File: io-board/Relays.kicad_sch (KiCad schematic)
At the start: 44 parts, among them K1 FRM18A-5 DC12V, K10 FRM18A-5 DC12V, K11 FRM18A-5 DC12V, K2 FRM18A-5 DC12V, K3 FRM18A-5 DC12V, K4 FRM18A-5 DC12V, K5 FRM18A-5 DC12V, K6 FRM18A-5 DC12V, K7 FRM18A-5 DC12V, K8 FRM18A-5 DC12V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

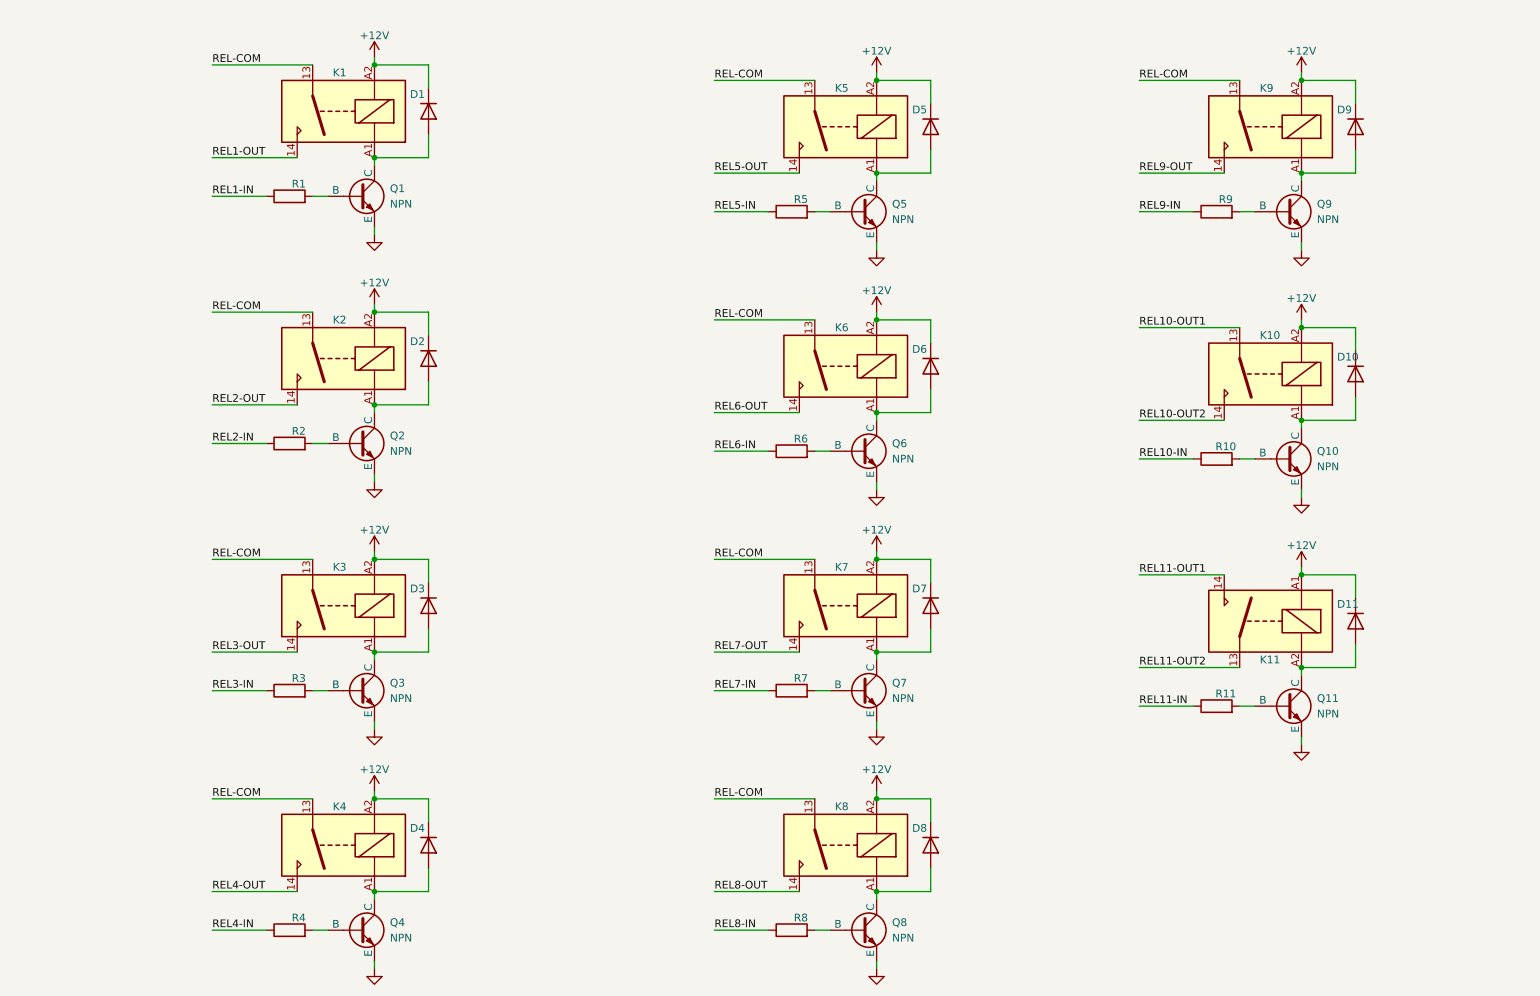
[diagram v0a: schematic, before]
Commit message: Add STM32 module
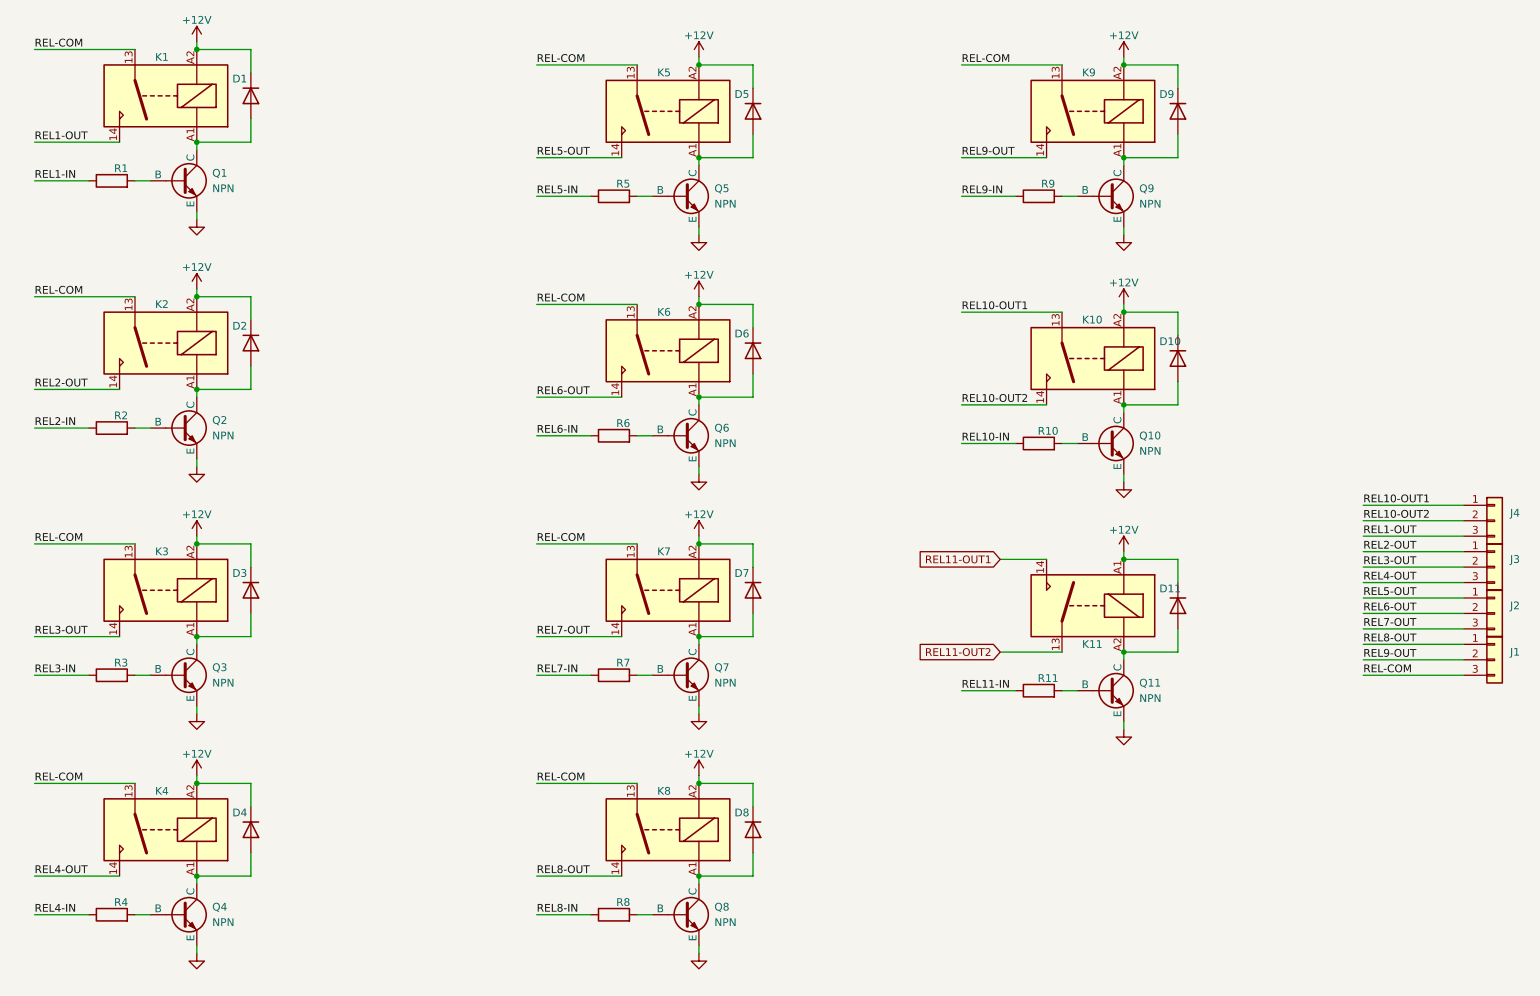
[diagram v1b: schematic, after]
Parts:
- added J1, J2, J3, J4: Conn_01x03, Footprints:DG128-5.0-03P-14-00A-H, symbol Connector_Generic:Conn_01x03
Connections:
- net REL-COM: now also J1.3 (Pin_3)
- net REL1-OUT: now also J4.3 (Pin_3)
- net REL10-OUT1: now also J4.1 (Pin_1)
- net REL10-OUT2: now also J4.2 (Pin_2)
- net REL2-OUT: now also J3.1 (Pin_1)
- net REL3-OUT: now also J3.2 (Pin_2)
- net REL4-OUT: now also J3.3 (Pin_3)
- net REL5-OUT: now also J2.1 (Pin_1)
- net REL6-OUT: now also J2.2 (Pin_2)
- net REL7-OUT: now also J2.3 (Pin_3)
- net REL8-OUT: now also J1.1 (Pin_1)
- net REL9-OUT: now also J1.2 (Pin_2)
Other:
- moved on the sheet: D1, D10, D11, D2, D3, D4, D5, D6, D7, D8, D9, K1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

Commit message: Almost all connected except OC and LED drivers
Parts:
- Q1, Q10, Q11, Q2, Q3, Q4, Q5, Q6, Q7, Q8, Q9: footprint Footprints:TO-92-3 -> Package_TO_SOT_SMD:SOT-23
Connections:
- net GND: now also Q1.2 (E), Q10.2 (E), Q11.2 (E), Q2.2 (E), Q3.2 (E), Q4.2 (E), Q5.2 (E), Q6.2 (E), Q7.2 (E), Q8.2 (E), Q9.2 (E); no longer Q1.3 (E), Q10.3 (E), Q11.3 (E), Q2.3 (E), Q3.3 (E), Q4.3 (E), Q5.3 (E), Q6.3 (E), Q7.3 (E), Q8.3 (E), Q9.3 (E)
- net at R10.2: now also Q10.1 (B); no longer Q10.2 (B)
- net at D5.2 (A), K5.A1: now also Q5.3 (C); no longer Q5.1 (C)
- net at R5.2: now also Q5.1 (B); no longer Q5.2 (B)
- net at R1.2: now also Q1.1 (B); no longer Q1.2 (B)
- net at D4.2 (A), K4.A1: now also Q4.3 (C); no longer Q4.1 (C)
- net at D2.2 (A), K2.A1: now also Q2.3 (C); no longer Q2.1 (C)
- net at D11.2 (A), K11.A2: now also Q11.3 (C); no longer Q11.1 (C)
- net at D1.2 (A), K1.A1: now also Q1.3 (C); no longer Q1.1 (C)
- net at R6.2: now also Q6.1 (B); no longer Q6.2 (B)
- net at D7.2 (A), K7.A1: now also Q7.3 (C); no longer Q7.1 (C)
- net at D9.2 (A), K9.A1: now also Q9.3 (C); no longer Q9.1 (C)
- net at R3.2: now also Q3.1 (B); no longer Q3.2 (B)
- net at D6.2 (A), K6.A1: now also Q6.3 (C); no longer Q6.1 (C)
- net at R9.2: now also Q9.1 (B); no longer Q9.2 (B)
- net at R7.2: now also Q7.1 (B); no longer Q7.2 (B)
- net at D8.2 (A), K8.A1: now also Q8.3 (C); no longer Q8.1 (C)
- net at R8.2: now also Q8.1 (B); no longer Q8.2 (B)
- net at D3.2 (A), K3.A1: now also Q3.3 (C); no longer Q3.1 (C)
- net at D10.2 (A), K10.A1: now also Q10.3 (C); no longer Q10.1 (C)
- net at R2.2: now also Q2.1 (B); no longer Q2.2 (B)
- net at R11.2: now also Q11.1 (B); no longer Q11.2 (B)
- net at R4.2: now also Q4.1 (B); no longer Q4.2 (B)

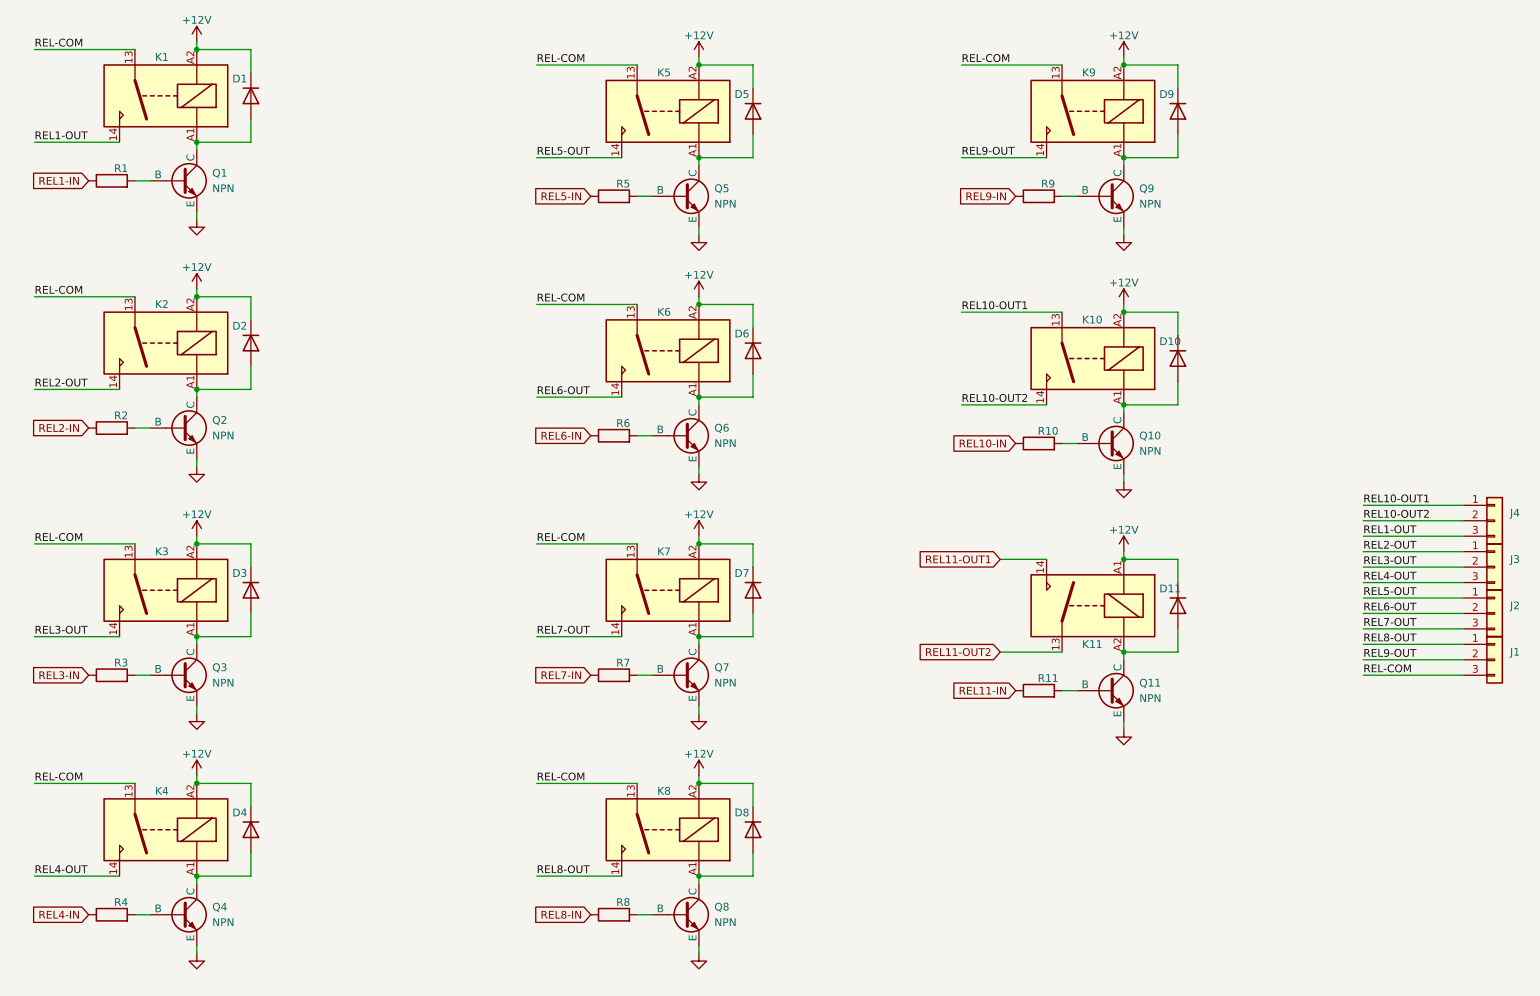
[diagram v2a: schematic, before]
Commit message: PCB: io-board: component values and BOM
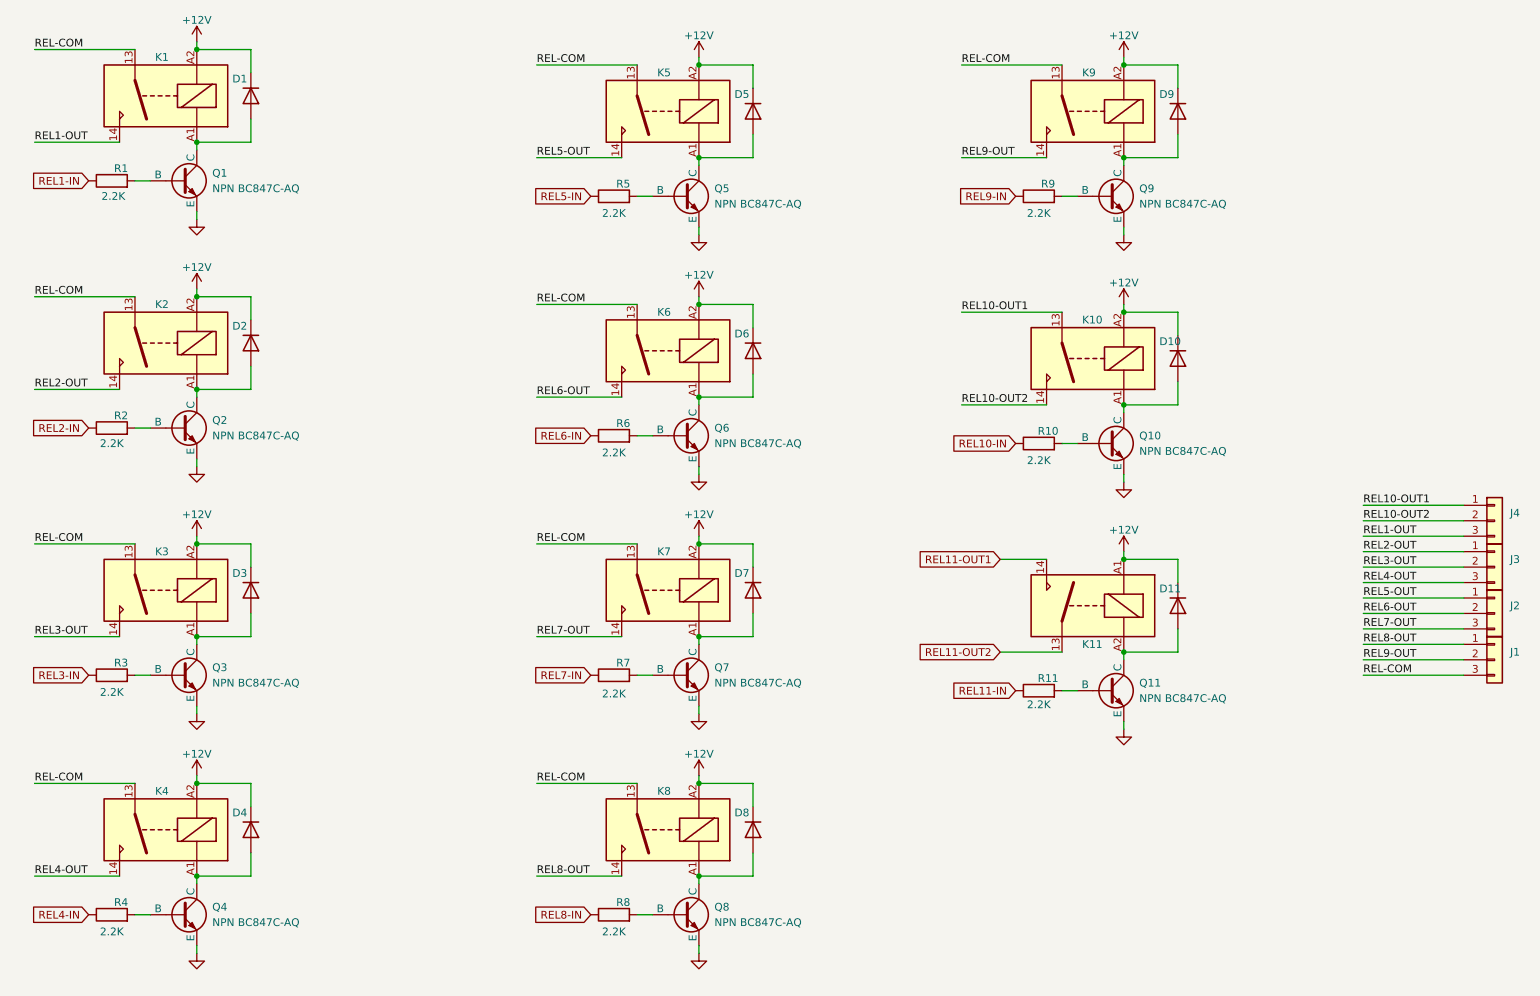
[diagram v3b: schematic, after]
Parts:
- D1, D10, D11, D2, D3, D4, D5, D6, D7, D8, D9: value D -> Vishay MCL4448-TR
- Q1, Q10, Q11, Q2, Q3, Q4, Q5, Q6, Q7, Q8, Q9: value NPN -> NPN BC847C-AQ
- R1, R10, R11, R2, R3, R4, R5, R6, R7, R8, R9: value R -> 2.2K
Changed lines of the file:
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@@
 			)
 		)
-		(property "Value" "R"
-			(at 189.992 89.408 90)
+		(property "Value" "2.2K"
+			(at 191.77 94.234 90)
 			(effects
 				(font
 					(size 1.27 1.27)
 				)
-				(hide yes)
 			)
 		)
@@
 			)
 		)
-		(property "Value" "R"
-			(at 37.592 46.228 90)
+		(property "Value" "2.2K"
+			(at 39.624 50.8 90)
 			(effects
 				(font
 					(size 1.27 1.27)
 				)
-				(hide yes)
 			)
 		)
@@
 			)
 		)
-		(property "Value" "D"
+		(property "Value" "Vishay MCL4448-TR"
 			(at 64.77 35.5599 90)
 			(effects
@@
 			)
 		)
-		(property "Value" "NPN"
+		(property "Value" "NPN BC847C-AQ"
 			(at 138.43 91.4399 0)
 			(effects
@@
 			)
 		)
-		(property "Value" "R"
-			(at 120.142 88.138 90)
+		(property "Value" "2.2K"
+			(at 121.92 92.964 90)
 			(effects
 				(font
 					(size 1.27 1.27)
 				)
-				(hide yes)
 			)
 		)
@@
 			)
 		)
-		(property "Value" "NPN"
+		(property "Value" "NPN BC847C-AQ"
 			(at 55.88 170.1799 0)
 			(effects
@@
 			)
 		)
-		(property "Value" "D"
+		(property "Value" "Vishay MCL4448-TR"
 			(at 217.17 38.0999 90)
 			(effects
@@
 			)
 		)
-		(property "Value" "NPN"
+		(property "Value" "NPN BC847C-AQ"
 			(at 208.28 52.0699 0)
 			(effects
@@
 			)
 		)
-		(property "Value" "NPN"
+		(property "Value" "NPN BC847C-AQ"
 			(at 208.28 133.3499 0)
 			(effects
@@
 			)
 		)
-		(property "Value" "R"
-			(at 37.592 127.508 90)
+		(property "Value" "2.2K"
+			(at 39.37 132.334 90)
 			(effects
 				(font
 					(size 1.27 1.27)
 				)
-				(hide yes)
 			)
 		)
@@
 			)
 		)
-		(property "Value" "D"
+		(property "Value" "Vishay MCL4448-TR"
 			(at 147.32 77.4699 90)
 			(effects
@@
 			)
 		)
-		(property "Value" "NPN"
+		(property "Value" "NPN BC847C-AQ"
 			(at 138.43 52.0699 0)
 			(effects
@@
 			)
 		)
-		(property "Value" "D"
+		(property "Value" "Vishay MCL4448-TR"
 			(at 217.17 119.3799 90)
 			(effects
@@
 			)
 		)
-		(property "Value" "NPN"
+		(property "Value" "NPN BC847C-AQ"
 			(at 138.43 130.8099 0)
 			(effects
@@
 			)
 		)
-		(property "Value" "D"
+		(property "Value" "Vishay MCL4448-TR"
 			(at 147.32 38.0999 90)
 			(effects
@@
 			)
 		)
-		(property "Value" "NPN"
+		(property "Value" "NPN BC847C-AQ"
 			(at 55.88 130.8099 0)
 			(effects
@@
 			)
 		)
-		(property "Value" "D"
+		(property "Value" "Vishay MCL4448-TR"
 			(at 217.17 78.7399 90)
 			(effects
@@
 			)
 		)
-		(property "Value" "D"
+		(property "Value" "Vishay MCL4448-TR"
 			(at 64.77 76.1999 90)
 			(effects
@@
 			)
 		)
-		(property "Value" "NPN"
+		(property "Value" "NPN BC847C-AQ"
 			(at 208.28 92.7099 0)
 			(effects
@@
 			)
 		)
-		(property "Value" "D"
+		(property "Value" "Vishay MCL4448-TR"
 			(at 64.77 116.8399 90)
 			(effects
@@
 			)
 		)
-		(property "Value" "NPN"
+		(property "Value" "NPN BC847C-AQ"
 			(at 55.88 90.1699 0)
 			(effects
@@
 			)
 		)
-		(property "Value" "R"
-			(at 120.142 48.768 90)
+		(property "Value" "2.2K"
+			(at 121.92 53.594 90)
 			(effects
 				(font
 					(size 1.27 1.27)
 				)
-				(hide yes)
 			)
 		)
@@
 			)
 		)
-		(property "Value" "NPN"
+		(property "Value" "NPN BC847C-AQ"
 			(at 55.88 49.5299 0)
 			(effects
@@
 			)
 		)
-		(property "Value" "R"
-			(at 120.142 166.878 90)
+		(property "Value" "2.2K"
+			(at 121.92 171.704 90)
 			(effects
 				(font
 					(size 1.27 1.27)
 				)
-				(hide yes)
 			)
 		)
@@
 			)
 		)
-		(property "Value" "D"
+		(property "Value" "Vishay MCL4448-TR"
 			(at 147.32 156.2099 90)
 			(effects
@@
 			)
 		)
-		(property "Value" "R"
-			(at 189.992 48.768 90)
+		(property "Value" "2.2K"
+			(at 191.77 53.594 90)
 			(effects
 				(font
 					(size 1.27 1.27)
 				)
-				(hide yes)
 			)
 		)
@@
 			)
 		)
-		(property "Value" "R"
-			(at 37.592 166.878 90)
+		(property "Value" "2.2K"
+			(at 39.37 171.704 90)
 			(effects
 				(font
 					(size 1.27 1.27)
 				)
-				(hide yes)
 			)
 		)
@@
 			)
 		)
-		(property "Value" "D"
+		(property "Value" "Vishay MCL4448-TR"
 			(at 147.32 116.8399 90)
 			(effects
@@
 			)
 		)
-		(property "Value" "D"
+		(property "Value" "Vishay MCL4448-TR"
 			(at 64.77 156.2099 90)
 			(effects
@@
 			)
 		)
-		(property "Value" "R"
-			(at 120.142 127.508 90)
+		(property "Value" "2.2K"
+			(at 121.92 132.588 90)
 			(effects
 				(font
 					(size 1.27 1.27)
 				)
-				(hide yes)
 			)
 		)
@@
 			)
 		)
-		(property "Value" "R"
-			(at 189.992 130.048 90)
+		(property "Value" "2.2K"
+			(at 191.77 134.366 90)
 			(effects
 				(font
 					(size 1.27 1.27)
 				)
-				(hide yes)
 			)
 		)
@@
 			)
 		)
-		(property "Value" "R"
-			(at 37.592 86.868 90)
+		(property "Value" "2.2K"
+			(at 39.37 91.44 90)
 			(effects
 				(font
 					(size 1.27 1.27)
 				)
-				(hide yes)
 			)
 		)
@@
 			)
 		)
-		(property "Value" "NPN"
+		(property "Value" "NPN BC847C-AQ"
 			(at 138.43 170.1799 0)
 			(effects
